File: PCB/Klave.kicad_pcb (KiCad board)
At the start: 2 copper layers, 81 parts, among them J1 6P6C, J2 OLED, SW0 Reset, SW1 0:0, SW10 1:3, SW11 1:4, SW12 1:5, SW13 2:0, SW14 2:1, SW15 2:2, SW16 2:3, SW17 2:4, SW18 2:5, SW19 3:0, SW2 0:1, SW20 3:1, SW21 3:2, SW22 3:3, SW23 3:4, SW24 3:5, SW26 4:1, SW27 4:2, SW28 4:3, SW29 4:4, SW3 0:2, SW30 4:5, SW35 5:4, SW36 5:5, SW4 0:3, SW5 0:4, SW6 0:5, SW7 1:0, SW8 1:1, SW9 1:2, U1 ProMicro

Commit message: Add edge cuts
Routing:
- net col5: track 182.2 -> 174.4 mm
- net row0: track 191.4 -> 193.5 mm
- added copper zone on B.Cu, net GND
- added copper zone on F.Cu, net GND
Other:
- board outline added: 157.7 x 128.7 mm
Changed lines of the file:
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@@
   (general
     (thickness 1.6)
-    (drawings 0)
-    (tracks 1025)
+    (drawings 16)
+    (tracks 1026)
     (zones 0)
     (modules 81)
@@
   (layers
     (0 F.Cu signal)
-    (31 B.Cu signal hide)
-    (32 B.Adhes user hide)
-    (33 F.Adhes user hide)
-    (34 B.Paste user hide)
+    (31 B.Cu signal)
+    (32 B.Adhes user)
+    (33 F.Adhes user)
+    (34 B.Paste user)
     (35 F.Paste user)
-    (36 B.SilkS user hide)
+    (36 B.SilkS user)
     (37 F.SilkS user)
-    (38 B.Mask user hide)
+    (38 B.Mask user)
     (39 F.Mask user)
-    (40 Dwgs.User user hide)
-    (41 Cmts.User user hide)
-    (42 Eco1.User user hide)
-    (43 Eco2.User user hide)
+    (40 Dwgs.User user)
+    (41 Cmts.User user)
+    (42 Eco1.User user)
+    (43 Eco2.User user)
     (44 Edge.Cuts user)
-    (45 Margin user hide)
+    (45 Margin user)
     (46 B.CrtYd user hide)
     (47 F.CrtYd user hide)
@@
     (at 151.4 45.8 90)
     (attr smd)
-    (fp_text reference R3 (at 3.6 -1.82 90) (layer F.SilkS)
+    (fp_text reference R3 (at 2.54 -1.82 90) (layer F.SilkS)
       (effects (font (size 1 1) (thickness 0.15)))
     )
@@
       (effects (font (size 1 1) (thickness 0.15)))
     )
-    (fp_text user %R (at 3.6 -1.82 90) (layer B.SilkS)
+    (fp_text user %R (at 2.54 -1.82 90) (layer B.SilkS)
       (effects (font (size 1 1) (thickness 0.15)) (justify mirror))
     )
@@
     )
   )
+  (gr_line (start 73.625 126.825) (end 73.625 132.525) (layer Edge.Cuts) (width 0.1))
+  (gr_line (start 105.45 27.075) (end 105.45 35.15) (layer Edge.Cuts) (width 0.1))
+  (gr_line (start 85.025 27.075) (end 105.45 27.075) (layer Edge.Cuts) (width 0.1))
+  (gr_line (start 66.025 31.825) (end 85.025 27.075) (layer Edge.Cuts) (width 0.1))
+  (gr_line (start 27.075 47.975) (end 66.025 31.825) (layer Edge.Cuts) (width 0.1))
+  (gr_line (start 27.075 126.825) (end 27.075 47.975) (layer Edge.Cuts) (width 0.1))
+  (gr_line (start 73.625 126.825) (end 27.075 126.825) (layer Edge.Cuts) (width 0.1))
+  (gr_line (start 113.05 132.525) (end 73.625 132.525) (layer Edge.Cuts) (width 0.1))
+  (gr_line (start 130.15 136.8) (end 113.05 132.525) (layer Edge.Cuts) (width 0.1))
+  (gr_line (start 165.3 155.8) (end 130.15 136.8) (layer Edge.Cuts) (width 0.1))
+  (gr_line (start 184.775 119.225) (end 165.3 155.8) (layer Edge.Cuts) (width 0.1))
+  (gr_line (start 164.35 108.3) (end 184.775 119.225) (layer Edge.Cuts) (width 0.1))
+  (gr_line (start 164.35 61.75) (end 164.35 108.3) (layer Edge.Cuts) (width 0.1))
+  (gr_line (start 177.65 61.75) (end 164.35 61.75) (layer Edge.Cuts) (width 0.1))
+  (gr_line (start 177.65 35.15) (end 177.65 61.75) (layer Edge.Cuts) (width 0.1))
+  (gr_line (start 105.45 35.15) (end 177.65 35.15) (layer Edge.Cuts) (width 0.1))
   (via (at 45.4 59.2) (size 0.8) (drill 0.4) (layers F.Cu B.Cu) (net 1))
   (segment (start 45.36 61.44) (end 45.36 59.24) (width 0.25) (layer B.Cu) (net 1))
@@
   (segment (start 126.91 109.51) (end 126.2 108.8) (width 0.25) (layer B.Cu) (net 41))
   (segment (start 126.2 108.8) (end 126.2 91) (width 0.25) (layer B.Cu) (net 41))
-  (segment (start 126.91 90.58) (end 128.735001 92.405001) (width 0.25) (layer B.Cu) (net 41))
-  (segment (start 128.735001 92.405001) (end 134.022261 92.405001) (width 0.25) (layer B.Cu) (net 41))
   (segment (start 161.8 120.18274) (end 161.8 125.4) (width 0.25) (layer B.Cu) (net 41))
   (segment (start 152.703734 142.154192) (end 152.703734 139.296266) (width 0.25) (layer B.Cu) (net 41))
@@
   (segment (start 113.125001 40.399999) (end 130.199999 40.399999) (width 0.25) (layer F.Cu) (net 42))
   (segment (start 112.2 41.325) (end 113.125001 40.399999) (width 0.25) (layer F.Cu) (net 42))
-  (segment (start 103.674999 32.799999) (end 94.200001 32.799999) (width 0.25) (layer F.Cu) (net 42))
   (segment (start 94.200001 32.799999) (end 93.2 33.8) (width 0.25) (layer F.Cu) (net 42))
   (segment (start 93.2 33.8) (end 78.8 33.8) (width 0.25) (layer F.Cu) (net 42))
@@
   (segment (start 133.474999 39.125001) (end 131.2 41.4) (width 0.25) (layer B.Cu) (net 42))
   (segment (start 153.212653 39.525) (end 152.812654 39.125001) (width 0.25) (layer B.Cu) (net 42))
-  (segment (start 112.2 41.325) (end 103.674999 32.799999) (width 0.25) (layer F.Cu) (net 42))
   (via (at 110.8 40) (size 0.8) (drill 0.4) (layers F.Cu B.Cu) (net 42))
   (segment (start 112.2 41.325) (end 112.125 41.325) (width 0.25) (layer B.Cu) (net 42))
@@
   (segment (start 36.2 54.625) (end 36.2 54.6) (width 0.25) (layer B.Cu) (net 42))
   (segment (start 36.2 54.6) (end 38 52.8) (width 0.25) (layer B.Cu) (net 42))
+  (segment (start 110.8 40) (end 106.975 40) (width 0.25) (layer F.Cu) (net 42))
+  (segment (start 103.525001 36.550001) (end 103.525001 32.799999) (width 0.25) (layer F.Cu) (net 42))
+  (segment (start 106.975 40) (end 103.525001 36.550001) (width 0.25) (layer F.Cu) (net 42))
+  (segment (start 103.525001 32.799999) (end 94.200001 32.799999) (width 0.25) (layer F.Cu) (net 42))
+  (segment (start 110.8 40) (end 112.1 41.3) (width 0.25) (layer F.Cu) (net 42))
   (segment (start 55.2 71.725) (end 37.875 71.725) (width 0.25) (layer F.Cu) (net 43))
   (segment (start 37.875 71.725) (end 36.2 73.4) (width 0.25) (layer F.Cu) (net 43))
@@
   (segment (start 154.2875 60.4) (end 154.2875 60.3125) (width 0.25) (layer B.Cu) (net 60))
   (segment (start 154.2875 60.3125) (end 155.8 58.8) (width 0.25) (layer B.Cu) (net 60))
+  (zone (net 34) (net_name GND) (layer F.Cu) (hatch edge 0.508)
+    (connect_pads (clearance 0.508))
+    (min_thickness 0.254)
+    (fill yes (arc_segments 32) (thermal_gap 0.508) (thermal_bridge_width 0.508))
+    (polygon
+      (pts
+        (xy 286.9 199.975) (xy 9.975 199.975) (xy 9.975 9.975) (xy 286.9 9.975)
+      )
+    )
+  )
+  (zone (net 34) (net_name GND) (layer B.Cu) (hatch edge 0.508)
+    (connect_pads (clearance 0.508))
+    (min_thickness 0.254)
+    (fill yes (arc_segments 32) (thermal_gap 0.508) (thermal_bridge_width 0.508))
+    (polygon
+      (pts
+        (xy 286.9 199.975) (xy 9.975 199.975) (xy 9.975 9.975) (xy 286.9 9.975)
+      )
+    )
+  )
 )

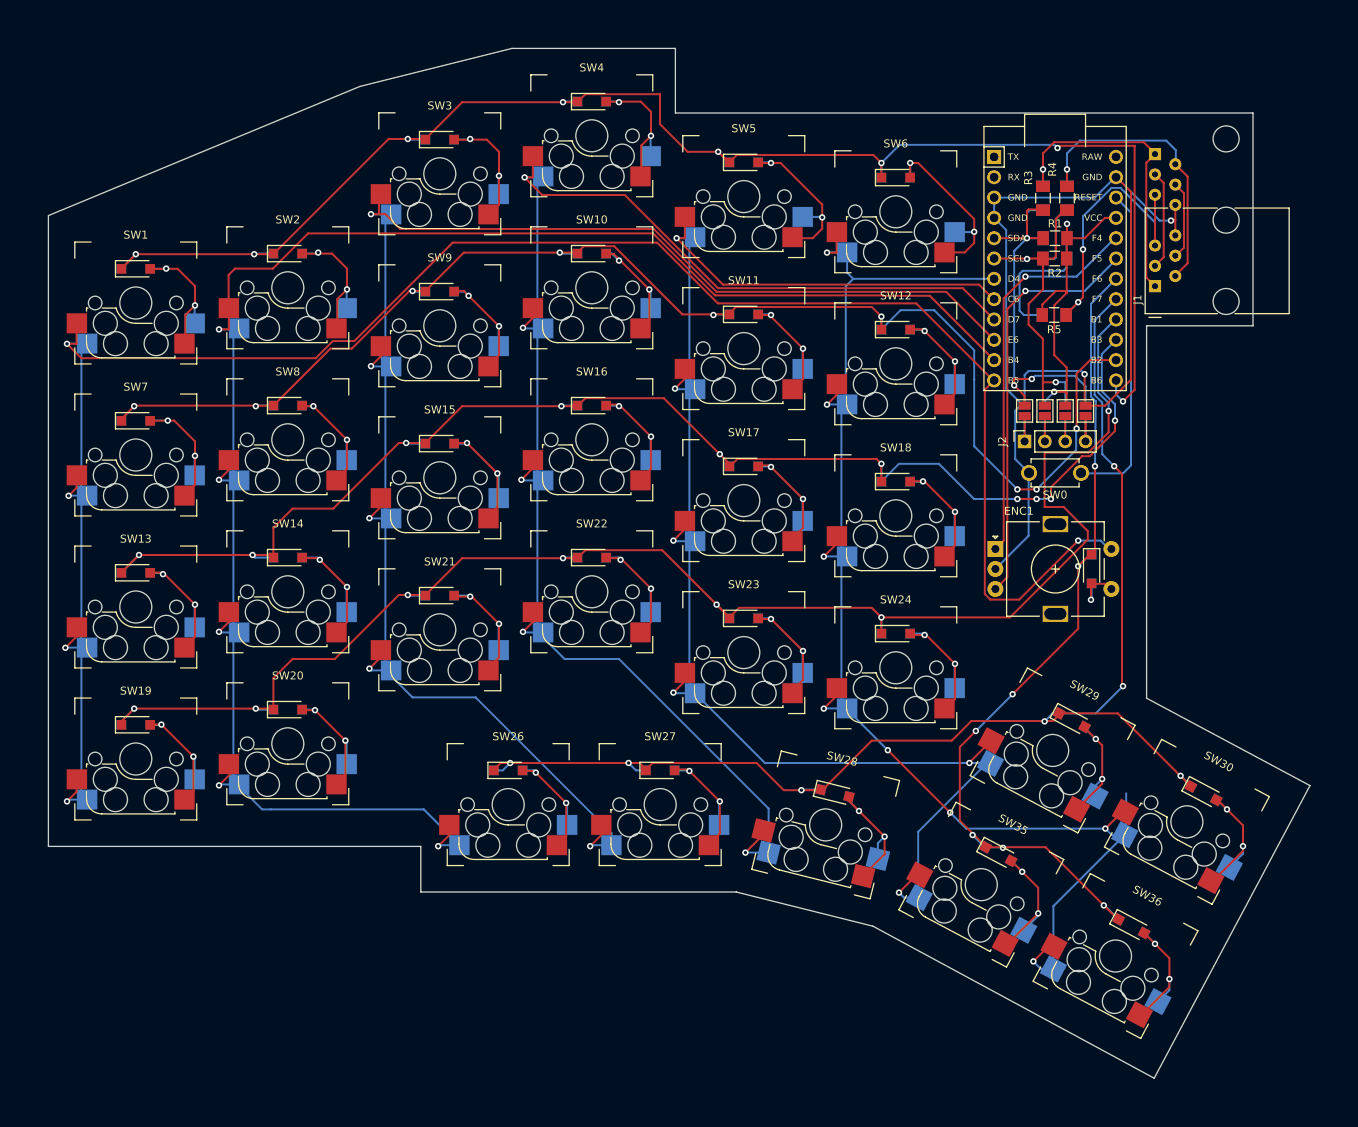
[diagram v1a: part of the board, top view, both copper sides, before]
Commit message: Improve PCB edge cuts
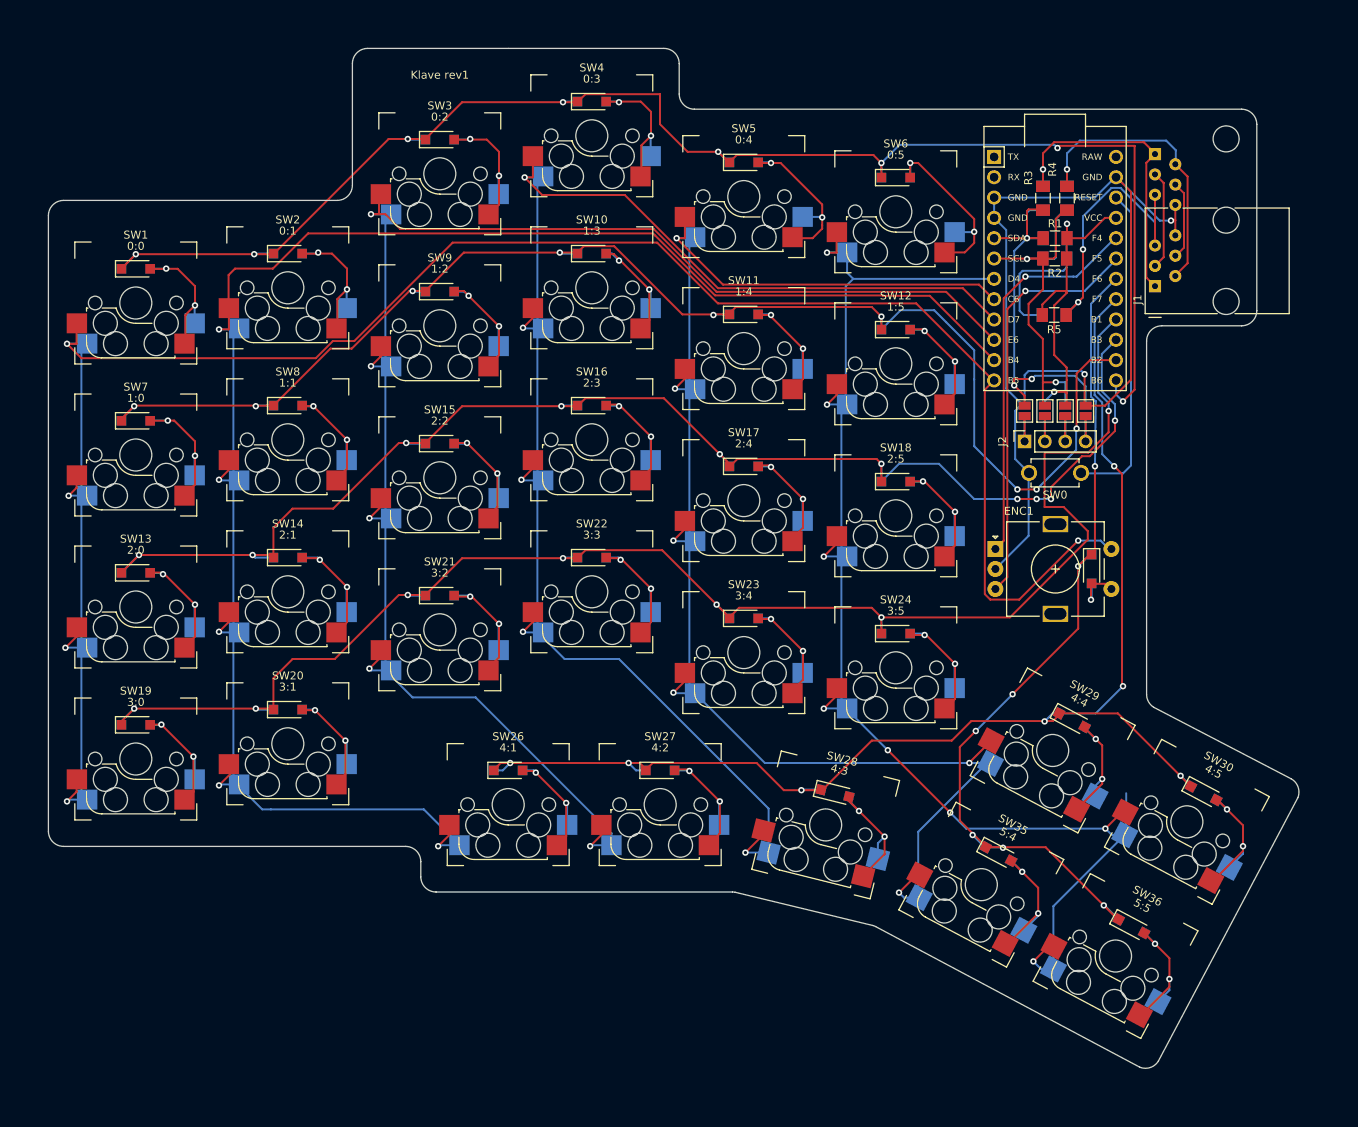
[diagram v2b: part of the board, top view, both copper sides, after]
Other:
- board size 157.7 x 128.7 mm -> 156.3 x 127.5 mm
- board text added: "Klave rev1"

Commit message: Improve PCB edge cuts and update footprints from library
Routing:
- net row0: track 193.5 -> 196.3 mm
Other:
- outline, holes or cut-outs redrawn

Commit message: Add mounting holes
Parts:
- added H1: MountingHole, KlaveLib:MountingHole_4.8mm_4.5mm, F.Cu at (47.0, 68.4)
- added H2: MountingHole, KlaveLib:MountingHole_4.8mm_4.5mm, F.Cu at (47.0, 106.4)
- added H3: MountingHole, KlaveLib:MountingHole_4.8mm_4.5mm, F.Cu at (85.0, 52.2)
- added H4: MountingHole, KlaveLib:MountingHole_4.8mm_4.5mm, F.Cu at (115.0, 114.0)
- added H5: MountingHole, KlaveLib:MountingHole_4.8mm_4.5mm, F.Cu at (124.0, 57.0)
- added H6: MountingHole, KlaveLib:MountingHole_4.8mm_4.5mm, F.Cu at (156.5, 127.7)
- renumbered Dr to D35
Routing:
- net col1: track 224.1 -> 229.8 mm
- net col5: track 174.4 -> 169.2 mm
- net col0: track 256.1 -> 259.8 mm
- net row1: track 181.1 -> 184.0 mm
- net col3: track 196.1 -> 198.3 mm
- net row5: track 110.3 -> 108.1 mm
- net row0: track 196.3 -> 194.5 mm
- net col2: track 207.6 -> 208.9 mm

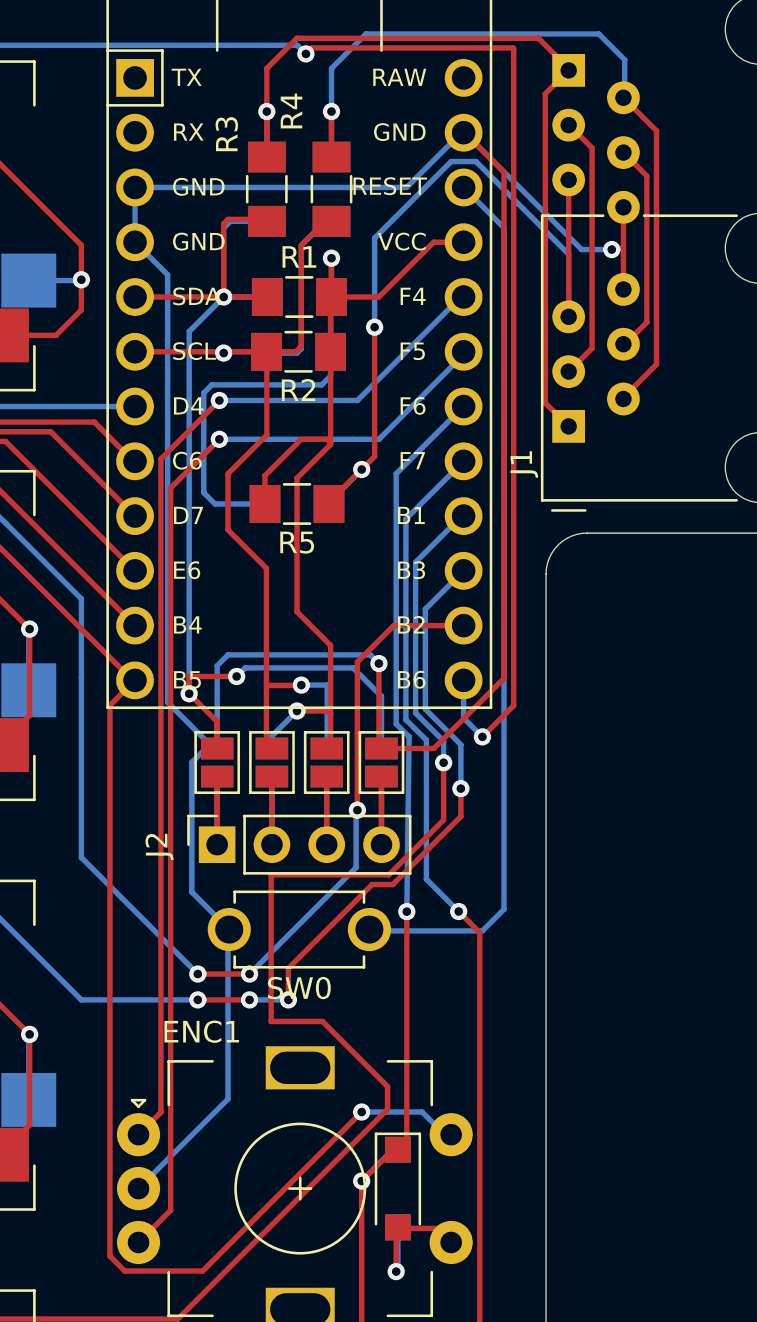
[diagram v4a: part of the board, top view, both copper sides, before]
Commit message: Add net class for power (VCC and GND)
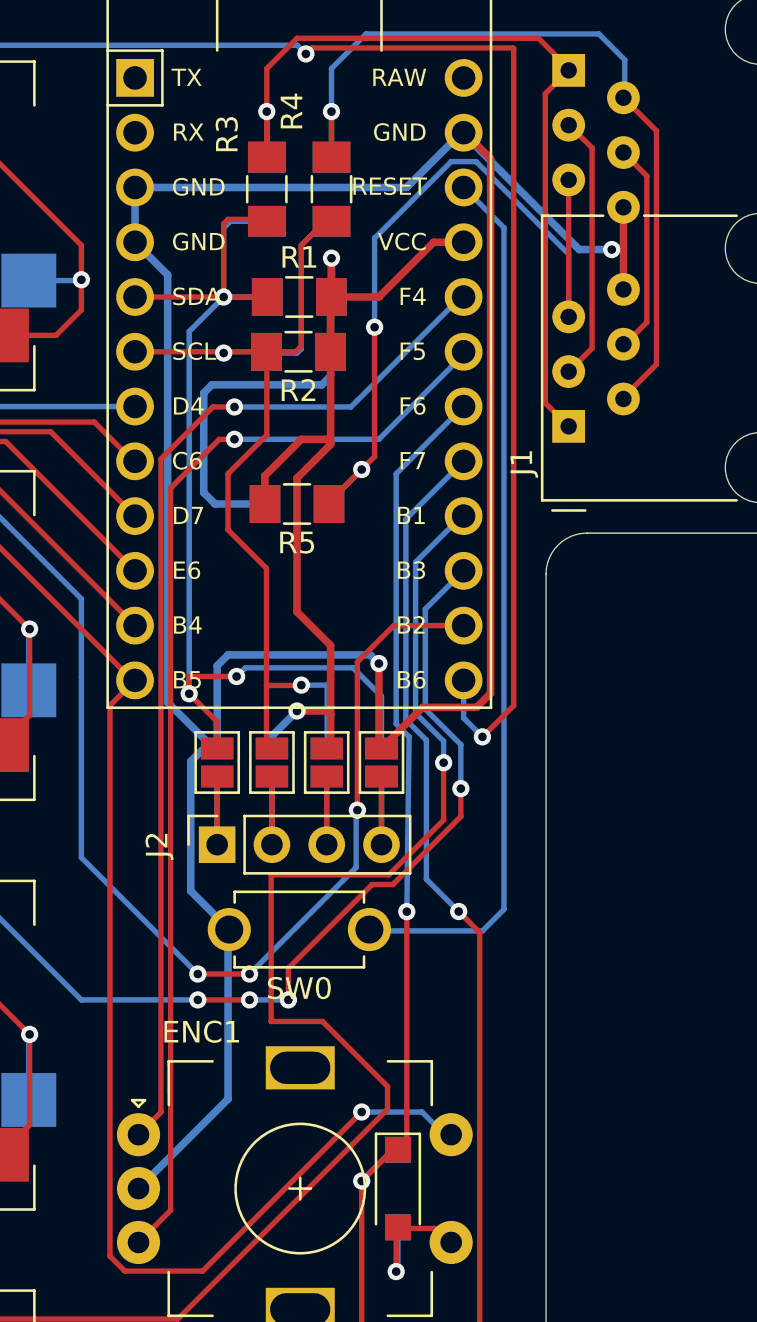
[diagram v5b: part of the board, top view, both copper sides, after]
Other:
- net class Power added: clearance 0.2, trace_width 0.35, via_dia 0.8, via_drill 0.4
